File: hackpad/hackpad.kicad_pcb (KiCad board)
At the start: 2 copper layers, 63.7 x 78.7 mm, 15 parts, among them SW1 SW_Push, SW10 SW_Push, SW2 SW_Push, SW3 SW_Push, SW4 SW_Push, SW5 SW_Push, SW6 SW_Push, SW7 SW_Push, SW9 SW_Push, U1 MOUDLE-SEEEDUINO-XIAO

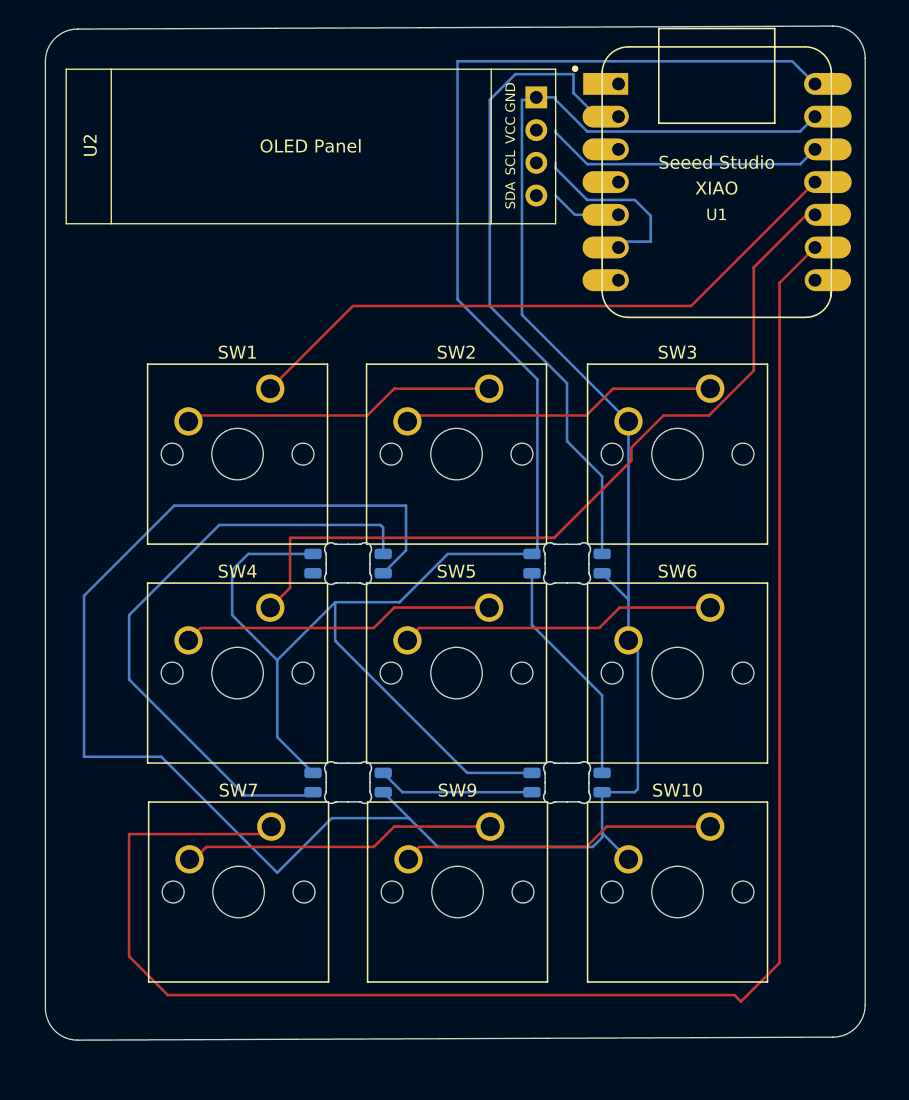
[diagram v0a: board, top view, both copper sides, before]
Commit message: Adjusted Firmware for diodes.
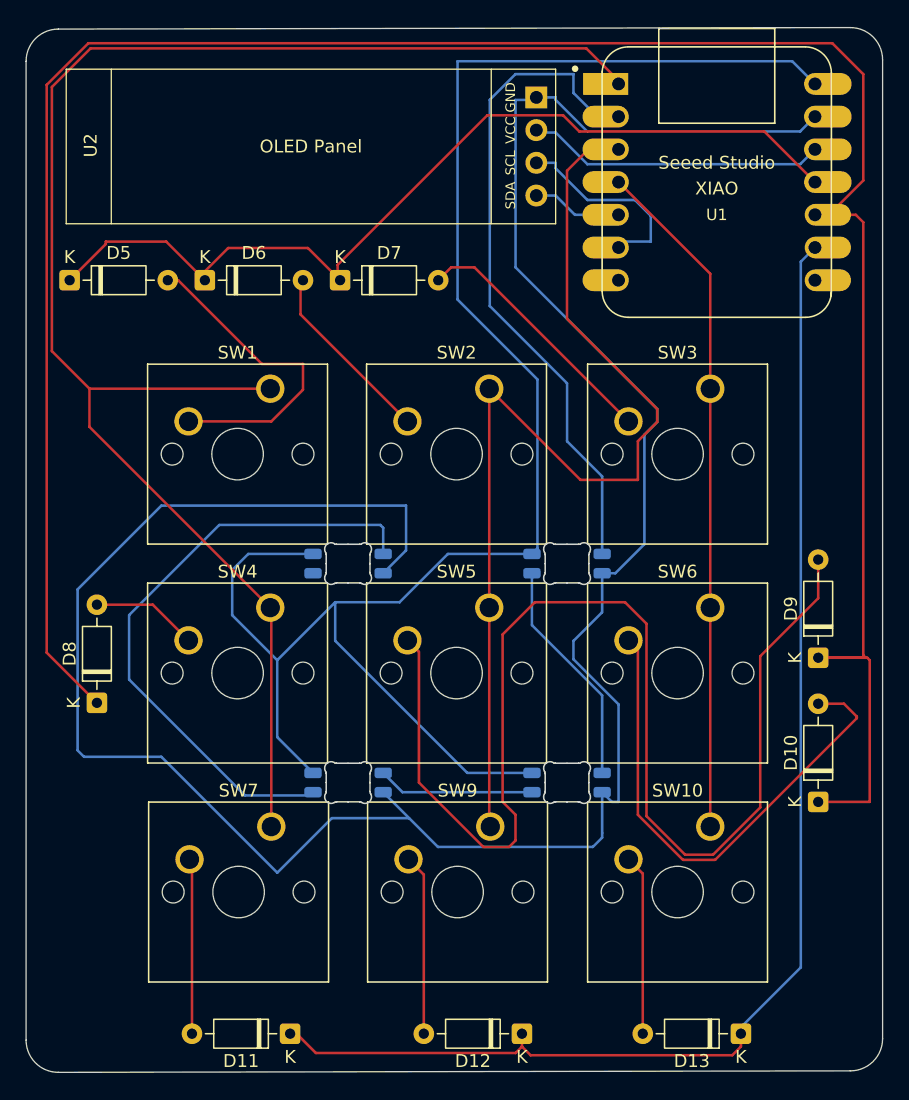
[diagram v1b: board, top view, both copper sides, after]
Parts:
- added D10: 1N4148, Diode_THT:D_DO-35_SOD27_P7.62mm_Horizontal, F.Cu at (212.0, 104.5)
- added D11: 1N4148, Diode_THT:D_DO-35_SOD27_P7.62mm_Horizontal, F.Cu at (171.0, 122.5)
- added D12: 1N4148, Diode_THT:D_DO-35_SOD27_P7.62mm_Horizontal, F.Cu at (189.0, 122.5)
- added D13: 1N4148, Diode_THT:D_DO-35_SOD27_P7.62mm_Horizontal, F.Cu at (206.0, 122.5)
- added D5: 1N4148, Diode_THT:D_DO-35_SOD27_P7.62mm_Horizontal, F.Cu at (153.9, 64.0)
- added D6: 1N4148, Diode_THT:D_DO-35_SOD27_P7.62mm_Horizontal, F.Cu at (164.4, 64.0)
- added D7: 1N4148, Diode_THT:D_DO-35_SOD27_P7.62mm_Horizontal, F.Cu at (174.9, 64.0)
- added D8: 1N4148, Diode_THT:D_DO-35_SOD27_P7.62mm_Horizontal, F.Cu at (156.0, 96.8)
- added D9: 1N4148, Diode_THT:D_DO-35_SOD27_P7.62mm_Horizontal, F.Cu at (212.0, 93.3)
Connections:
- SW1 pad 1: Net-(U1-PA6_A10_D10_MOSI) -> /col1
- SW1 pad 2: Net-(SW1-Pad2) -> Net-(D5-A)
- SW10 pad 1: Net-(SW10-Pad1) -> /col3
- SW10 pad 2: GND -> Net-(D13-A)
- SW2 pad 1: Net-(SW1-Pad2) -> /col2
- SW2 pad 2: Net-(SW2-Pad2) -> Net-(D6-A)
- SW3 pad 1: Net-(SW2-Pad2) -> /col3
- SW3 pad 2: GND -> Net-(D7-A)
- SW4 pad 1: Net-(U1-PA5_A9_D9_MISO) -> /col1
- SW4 pad 2: Net-(SW4-Pad2) -> Net-(D8-A)
- SW5 pad 1: Net-(SW4-Pad2) -> /col2
- SW5 pad 2: Net-(SW5-Pad2) -> Net-(D9-A)
- SW6 pad 1: Net-(SW5-Pad2) -> /col3
- SW6 pad 2: GND -> Net-(D10-A)
- SW7 pad 1: Net-(U1-PA7_A8_D8_SCK) -> /col1
- SW7 pad 2: Net-(SW7-Pad2) -> Net-(D11-A)
- SW9 pad 1: Net-(SW7-Pad2) -> /col2
- SW9 pad 2: Net-(SW10-Pad1) -> Net-(D12-A)
- U1 pad 1: unconnected-(U1-PA02_A0_D0-Pad1) -> /col1
- U1 pad 10: Net-(U1-PA5_A9_D9_MISO) -> Net-(D10-K)
- U1 pad 11: Net-(U1-PA6_A10_D10_MOSI) -> Net-(D5-K)
- U1 pad 3: unconnected-(U1-PA10_A2_D2-Pad3) -> /col2
- U1 pad 4: unconnected-(U1-PA11_A3_D3-Pad4) -> /col3
- U1 pad 9: Net-(U1-PA7_A8_D8_SCK) -> Net-(D11-K)
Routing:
- net Net-(D10-K): track 0.00 -> 189.1 mm
- net Net-(U1-PA7_A8_D8_SCK): track 130.7 -> 0.00 mm
- net /col1: track 0.00 -> 125.1 mm
- net Net-(D11-K): track 0.00 -> 101.8 mm
- net Net-(D9-A): track 0.00 -> 98.1 mm
- net /col2: track 0.00 -> 80.7 mm
- net Net-(D5-K): track 0.00 -> 71.4 mm
- net Net-(U1-PA5_A9_D9_MISO): track 62.5 -> 0.00 mm
- net /col3: track 0.00 -> 54.0 mm
- net Net-(U1-PA6_A10_D10_MOSI): track 48.9 -> 0.00 mm
- net Net-(D10-A): track 0.00 -> 41.4 mm
- net Net-(D5-A): track 0.00 -> 25.1 mm
- net Net-(SW5-Pad2): track 24.6 -> 0.00 mm
- net Net-(SW10-Pad1): track 24.6 -> 0.00 mm
- net Net-(SW2-Pad2): track 24.6 -> 0.00 mm
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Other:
- board size 63.7 x 78.7 mm -> 66.5 x 81.1 mm
